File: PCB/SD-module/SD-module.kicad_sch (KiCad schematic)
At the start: 12 parts, among them J1 Connector, K1 SD-106M, U1 SE5218, U2 TXB0104PWR

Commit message: More OCD
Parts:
- K1: JLC_3DModel (none) -> c5caca3680b94ec08f0c91dd89c79f9f; JLC_3D_Size (none) -> 28.7 30.4
- renumbered C3 to C1, C4 to C3, C1 to C4, C6 to C5, C5 to C6
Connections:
- net GND: now also K1.12 (SHELL), K1.13 (SHELL)
- no-connect marks 3 -> 6
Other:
- moved on the sheet: C5, C6, C7

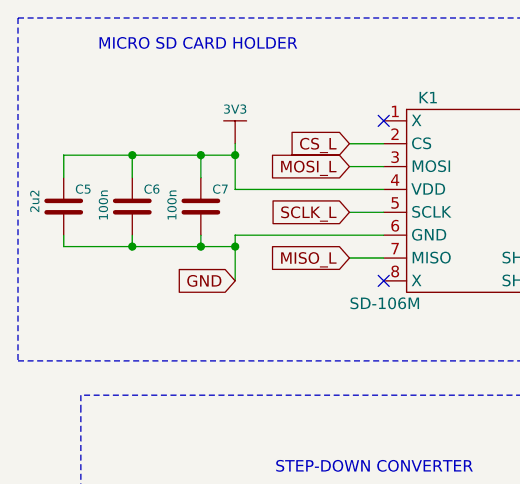
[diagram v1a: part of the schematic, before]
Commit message: Fix microSD caps
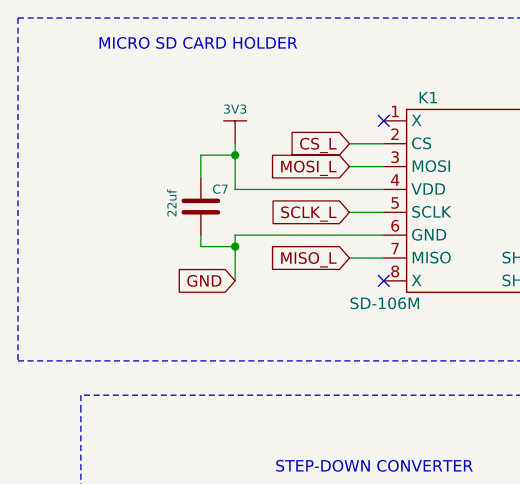
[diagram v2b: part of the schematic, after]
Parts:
- removed C5: 2u2, Capacitor_SMD:C_0603_1608Metric, symbol e-radionica.com schematics:0603C
- removed C6: 100n, Capacitor_SMD:C_0603_1608Metric, symbol e-radionica.com schematics:0603C
- C7: value 100n -> 22uf; LCSC C1590 -> C45783

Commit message: fatter traces
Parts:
- C7: footprint Capacitor_SMD:C_0603_1608Metric -> Capacitor_SMD:C_0805_2012Metric
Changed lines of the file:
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@@
 			)
 		)
-		(property "Footprint" "Capacitor_SMD:C_0603_1608Metric"
+		(property "Footprint" "Capacitor_SMD:C_0805_2012Metric"
 			(at 66.04 46.355 0)
 			(effects

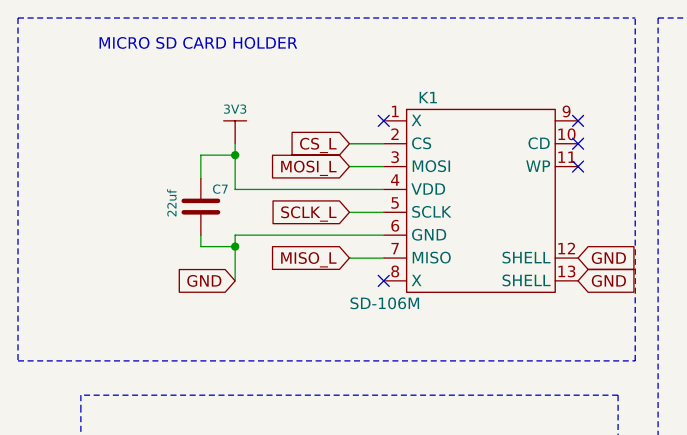
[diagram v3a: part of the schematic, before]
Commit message: Fix SD module pins
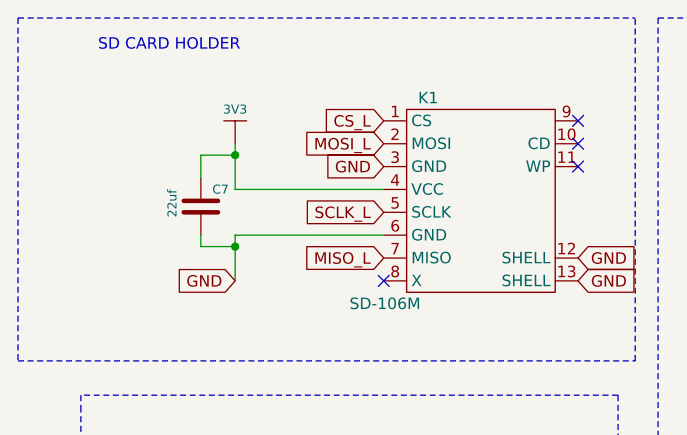
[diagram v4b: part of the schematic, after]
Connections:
- net CS_L: now also K1.1 (CS); no longer K1.2 (CS)
- net GND: now also K1.3 (GND)
- net MOSI_L: now also K1.2 (MOSI); no longer K1.3 (MOSI)
- no-connect marks 6 -> 5
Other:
- note added: "SD CARD HOLDER"
- note removed: "MICRO SD CARD HOLDER"
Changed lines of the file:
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@@
 		)
 	)
-	(text "MICRO SD CARD HOLDER"
+	(text "SD CARD HOLDER"
 		(exclude_from_sim no)
 		(at 54.61 29.21 0)
@@
 		(at 107.95 39.37)
 	)
-	(no_connect
-		(at 86.36 36.83)
-	)
 	(polyline
 		(pts
@@
 	(wire
 		(pts
-			(xy 82.55 52.07) (xy 86.36 52.07)
-		)
-		(stroke
-			(width 0)
-			(type solid)
-		)
-	)
-	(wire
-		(pts
 			(xy 154.94 70.485) (xy 154.94 72.39)
 		)
@@
 	(wire
 		(pts
-			(xy 82.55 46.99) (xy 86.36 46.99)
-		)
-		(stroke
-			(width 0)
-			(type solid)
-		)
-	)
-	(wire
-		(pts
 			(xy 152.4 49.53) (xy 158.75 49.53)
 		)
@@
 	(wire
 		(pts
-			(xy 82.55 41.91) (xy 86.36 41.91)
-		)
-		(stroke
-			(width 0)
-			(type solid)
-		)
-	)
-	(wire
-		(pts
 			(xy 72.39 102.87) (xy 72.39 110.49)
 		)
@@
 		)
 	)
-	(wire
-		(pts
-			(xy 82.55 39.37) (xy 86.36 39.37)
-		)
-		(stroke
-			(width 0)
-			(type solid)
-		)
-	)
 	(global_label "GND"
 		(shape input)
@@
 	(global_label "CS_L"
 		(shape input)
-		(at 82.55 39.37 180)
+		(at 86.36 36.83 180)
 		(fields_autoplaced yes)
 		(effects
@@
 		)
 		(property "Intersheetrefs" "${INTERSHEET_REFS}"
-			(at 75.6617 39.2906 0)
+			(at 79.4717 36.7506 0)
 			(effects
 				(font
@@
 		)
 	)
+	(global_label "GND"
+		(shape input)
+		(at 86.36 41.91 180)
+		(fields_autoplaced yes)
+		(effects
+			(font
+				(size 1.27 1.27)
+			)
+			(justify right)
+		)
+		(property "Intersheetrefs" "${INTERSHEET_REFS}"
+			(at 79.5043 41.91 0)
+			(effects
+				(font
+					(size 1.27 1.27)
+				)
+				(justify right)
+				(hide yes)
+			)
+		)
+	)
 	(global_label "CS"
 		(shape input)
@@
 	(global_label "MISO_L"
 		(shape input)
-		(at 82.55 52.07 180)
+		(at 86.36 52.07 180)
 		(fields_autoplaced yes)
 		(effects
@@
 		)
 		(property "Intersheetrefs" "${INTERSHEET_REFS}"
-			(at 73.545 51.9906 0)
+			(at 77.355 51.9906 0)
 			(effects
 				(font
@@
 	(global_label "MOSI_L"
 		(shape input)
-		(at 82.55 41.91 180)
+		(at 86.36 39.37 180)
 		(fields_autoplaced yes)
 		(effects
@@
 		)
 		(property "Intersheetrefs" "${INTERSHEET_REFS}"
-			(at 73.545 41.8306 0)
+			(at 77.355 39.2906 0)
 			(effects
 				(font
@@
 	(global_label "SCLK_L"
 		(shape input)
-		(at 82.55 46.99 180)
+		(at 86.36 46.99 180)
 		(fields_autoplaced yes)
 		(effects
@@
 		)
 		(property "Intersheetrefs" "${INTERSHEET_REFS}"
-			(at 73.3636 46.9106 0)
-			(effects
-				(font
+			(at 77.1736 46.9106 0)
+			(effects
+				(font

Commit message: Update details
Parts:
- U1: value SE5218 -> SE5218ALG-LF
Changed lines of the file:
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@@
-	)
-	(junction
-		(at 95.25 87.63)
-		(diameter 0.9144)
-		(color 0 0 0 0)
 	)
 	(junction
@@
 	)
 	(junction
-		(at 69.85 87.63)
-		(diameter 0.9144)
-		(color 0 0 0 0)
-	)
-	(junction
 		(at 144.78 38.1)
 		(diameter 0)
@@
 		)
 	)
-	(wire
-		(pts
-			(xy 69.85 87.63) (xy 78.74 87.63)
-		)
-		(stroke
-			(width 0)
-			(type solid)
-		)
-	)
 	(polyline
 		(pts
@@
 	(wire
 		(pts
-			(xy 69.85 87.63) (xy 69.85 100.33)
-		)
-		(stroke
-			(width 0)
-			(type solid)
-		)
-	)
-	(wire
-		(pts
-			(xy 95.25 87.63) (xy 95.25 100.33)
+			(xy 69.85 83.82) (xy 69.85 100.33)
+		)
+		(stroke
+			(width 0)
+			(type solid)
+		)
+	)
+	(wire
+		(pts
+			(xy 95.25 83.82) (xy 95.25 100.33)
 		)
 		(stroke
@@
 	(wire
 		(pts
-			(xy 86.36 87.63) (xy 95.25 87.63)
-		)
-		(stroke
-			(width 0)
-			(type solid)
-		)
-	)
-	(wire
-		(pts
 			(xy 132.08 38.1) (xy 132.08 46.99)
 		)
@@
 		)
 	)
-	(wire
-		(pts
-			(xy 95.25 87.63) (xy 95.25 83.82)
-		)
-		(stroke
-			(width 0)
-			(type solid)
-		)
-	)
 	(polyline
 		(pts
@@
 			(width 0)
 			(type dash)
-		)
-	)
-	(wire
-		(pts
-			(xy 69.85 83.82) (xy 69.85 87.63)
-		)
-		(stroke
-			(width 0)
-			(type solid)
 		)
 	)
@@
 			)
 		)
-		(property "Value" "SE5218"
+		(property "Value" "SE5218ALG-LF"
 			(at 82.55 107.95 0)
 			(effects
